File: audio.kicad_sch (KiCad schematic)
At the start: 14 parts

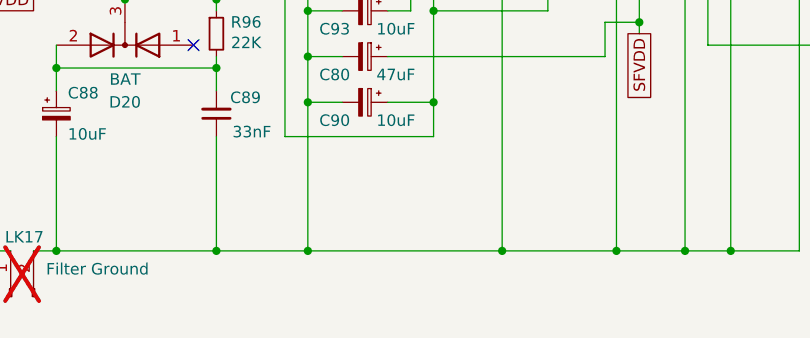
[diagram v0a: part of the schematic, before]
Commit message: add cheeky mean well power swap
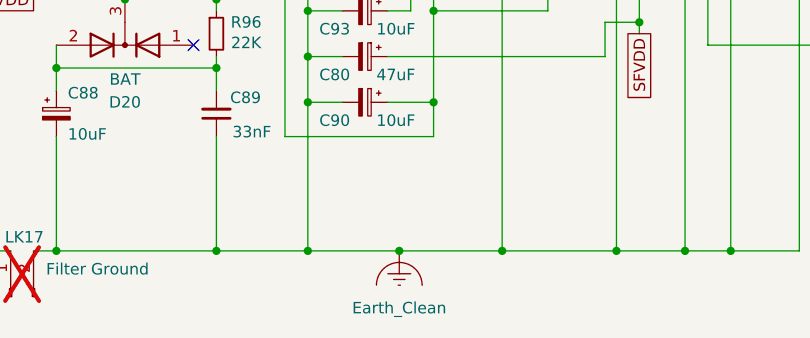
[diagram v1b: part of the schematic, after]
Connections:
- net Earth_Clean: now reaches C80.2, C88.2, C89.1, C90.2, C93.2, IM2.10 (Pin_10), IM2.13 (Pin_13), IM2.15 (Pin_15), IM2.18 (Pin_18), IM2.5 (Pin_5), LK17.2 (Pin_2), R212.2
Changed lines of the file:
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@@
+		(color 0 0 0 0)
+	)
+	(junction
+		(at 121.92 106.68)
+		(diameter 0)
 		(color 0 0 0 0)
 	)
@@
 	(wire
 		(pts
+			(xy 121.92 106.68) (xy 133.35 106.68)
+		)
+		(stroke
+			(width 0)
+			(type default)
+		)
+	)
+	(wire
+		(pts
 			(xy 166.37 66.04) (xy 166.37 106.68)
 		)
@@
 	(wire
 		(pts
-			(xy 111.76 106.68) (xy 133.35 106.68)
+			(xy 111.76 106.68) (xy 121.92 106.68)
 		)
 		(stroke
@@
 					(unit 1)
 				)
+			)
+		)
+	)
+	(symbol
+		(lib_id "power:Earth_Clean")
+		(at 121.92 106.68 0)
+		(unit 1)
+		(exclude_from_sim no)
+		(in_bom yes)
+		(on_board yes)
+		(dnp no)
+		(fields_autoplaced yes)
+		(property "Reference" "#PWR0199"
+			(at 121.92 114.3 0)
+			(effects
+				(font
+					(size 1.27 1.27)
+				)
+				(hide yes)
+			)
+		)
+		(property "Value" "Earth_Clean"
+			(at 121.92 113.03 0)
+			(effects
+				(font
+					(size 1.27 1.27)
+				)
+			)
+		)
+		(property "Footprint" ""
+			(at 121.92 107.95 0)
+			(effects
+				(font
+					(size 1.27 1.27)
+				)
+				(hide yes)
+			)
+		)
+		(property "Datasheet" "~"
+			(at 121.92 107.95 0)
+			(effects
+				(font
+					(size 1.27 1.27)
+				)
+				(hide yes)
+			)
+		)
+		(property "Description" "Power symbol creates a global label with name \"Earth_Clean\""
+			(at 121.92 106.68 0)
+			(effects
+				(font
+					(size 1.27 1.27)
+				)
+				(hide yes)
+			)
+		)
+		(pin "1"
+		)
+		(instances
+			(project "Acorn-A3010"
+				(path "/999882f3-94f8-4a89-9093-27a47d0cb289/0f9e4e4c-7eae-43dc-ad37-0c70003f4236"
+					(reference "#PWR0199")
+					(unit 1)
+				)

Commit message: fix port reference locations and lock components
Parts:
- C88, C90: footprint Capacitor_THT:CP_Radial_D4.0mm_P2.00mm -> Capacitor_THT:CP_Radial_D5.0mm_P2.50mm
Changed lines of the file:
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@@
 			)
 		)
-		(property "Footprint" "Capacitor_THT:CP_Radial_D4.0mm_P2.00mm"
+		(property "Footprint" "Capacitor_THT:CP_Radial_D5.0mm_P2.50mm"
 			(at 83.82 91.44 0)
 			(effects
@@
 			)
 		)
-		(property "Footprint" "Capacitor_THT:CP_Radial_D4.0mm_P2.00mm"
+		(property "Footprint" "Capacitor_THT:CP_Radial_D5.0mm_P2.50mm"
 			(at 118.11 90.17 0)
 			(effects

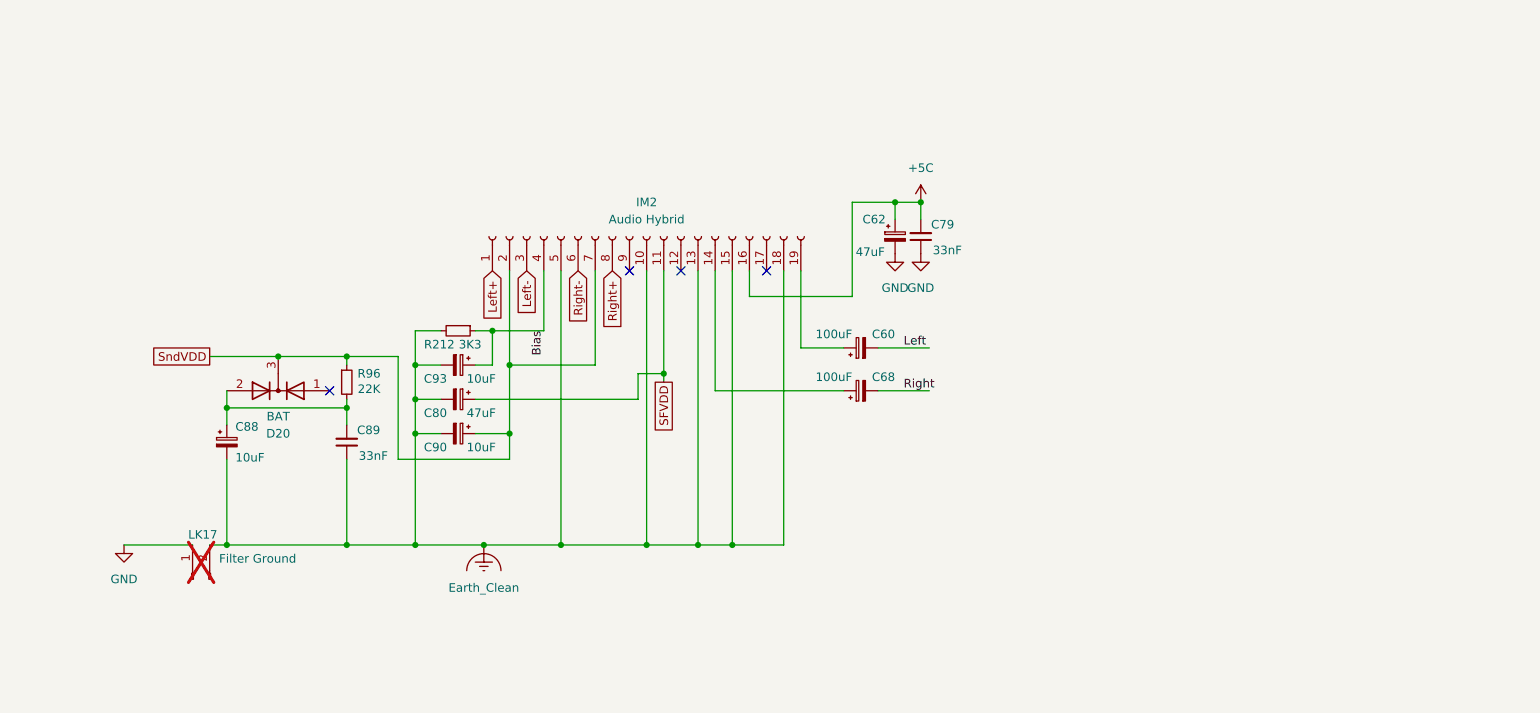
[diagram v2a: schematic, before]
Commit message: fix perimter port positions
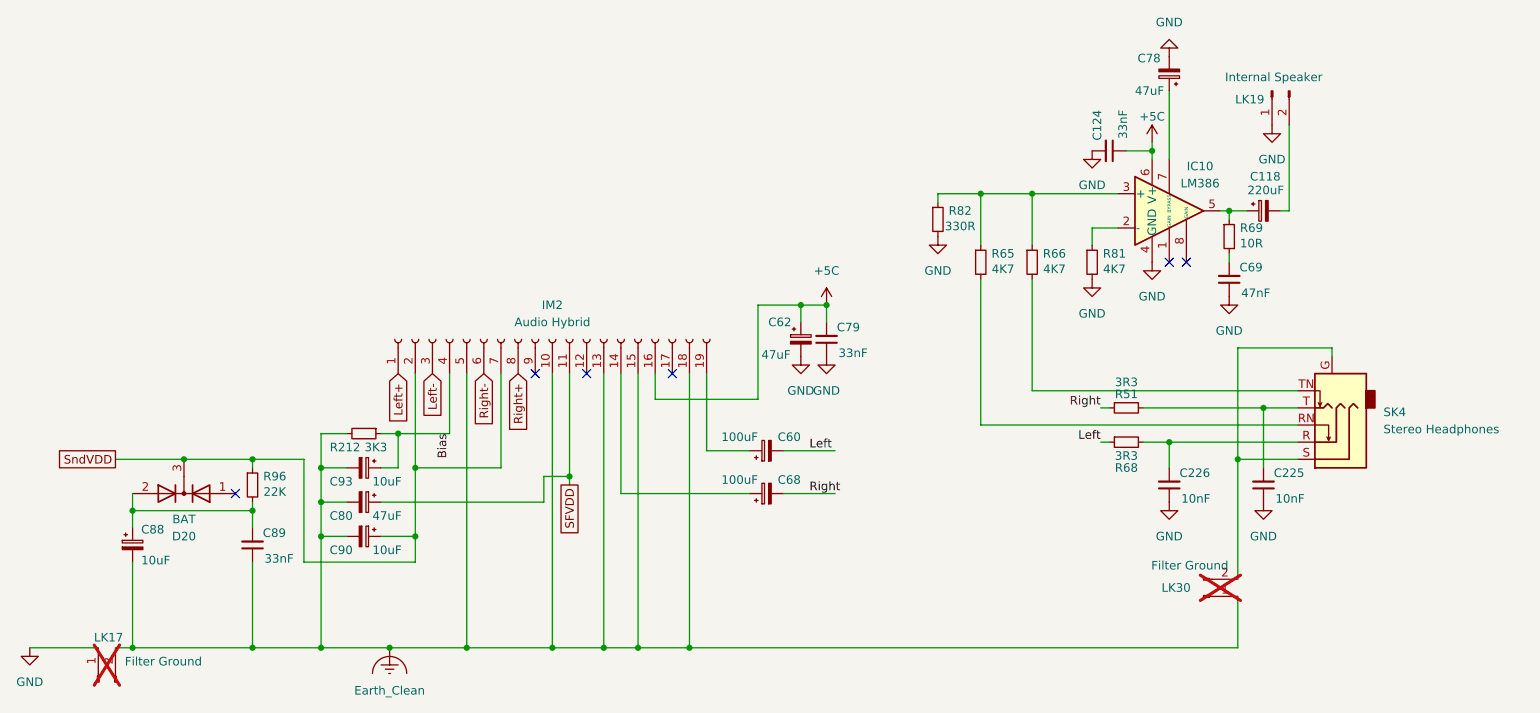
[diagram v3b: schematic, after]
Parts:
- added C118: 220uF, Capacitor_THT:CP_Radial_D8.0mm_P5.00mm, symbol Device:C_Polarized_Small
- added C124: 33nF, Capacitor_SMD:C_0805_2012Metric, symbol Device:C_Small
- added C225, C226: 10nF, Capacitor_SMD:C_0805_2012Metric, symbol Device:C_Small
- added C69: 47nF, Capacitor_SMD:C_0805_2012Metric, symbol Device:C_Small
- added C78: 47uF, Capacitor_THT:CP_Radial_D8.0mm_P5.00mm, symbol Device:C_Polarized_Small
- added IC10: LM386, Package_SO:SOIC-8_3.9x4.9mm_P1.27mm, symbol Amplifier_Audio:LM386
- added LK19: Internal Speaker, Connector_PinHeader_2.54mm:PinHeader_1x02_P2.54mm_Vertical, symbol Connector:Conn_01x02_Pin
- added LK30: Filter Ground, Connector_PinHeader_2.54mm:PinHeader_1x02_P2.54mm_Vertical, symbol Connector:Conn_01x02_Pin
- added R51, R68: 3R3, Resistor_SMD:R_0805_2012Metric, symbol Device:R_Small
- added R65, R66, R81: 4K7, Resistor_SMD:R_0805_2012Metric, symbol Device:R_Small
- added R69: 10R, Resistor_SMD:R_0805_2012Metric, symbol Device:R_Small
- added R82: 330R, Resistor_SMD:R_0805_2012Metric, symbol Device:R_Small
- added SK4: Stereo Headphones, Acorn:Jack_3.5mm_CUI_SJ1-3525N_Horizontal, symbol Connector_Audio:AudioJack3_Ground_SwitchTR
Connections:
- net +5C: now also C124.1, IC10.6 (V+)
- net Earth_Clean: now also LK30.1 (Pin_1)
- net GND: now also C124.2, C225.1, C226.1, C69.1, C78.2, IC10.4 (GND), LK19.1 (Pin_1), R81.2, R82.2
- net Left: now also R68.1
- net Right: now also R51.1
- new net: C225.2, R51.2, SK4.T
- new net: C69.2, R69.2
- new net: IC10.3 (+), R65.1, R66.1, R82.1
- new net: R65.2, SK4.RN
- new net: C118.1, IC10.5, R69.1
- new net: C118.2, LK19.2 (Pin_2)
- new net: R66.2, SK4.TN
- new net: IC10.2 (-), R81.1
- new net: C78.1, IC10.7 (BYPASS)
- new net: LK30.2 (Pin_2), SK4.G, SK4.S
- new net: C226.2, R68.2, SK4.R
- no-connect marks 4 -> 6
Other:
- moved on the sheet: C60, C62, C68, C79, C80, C88, C89, C90, C93, D20, IM2, LK17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

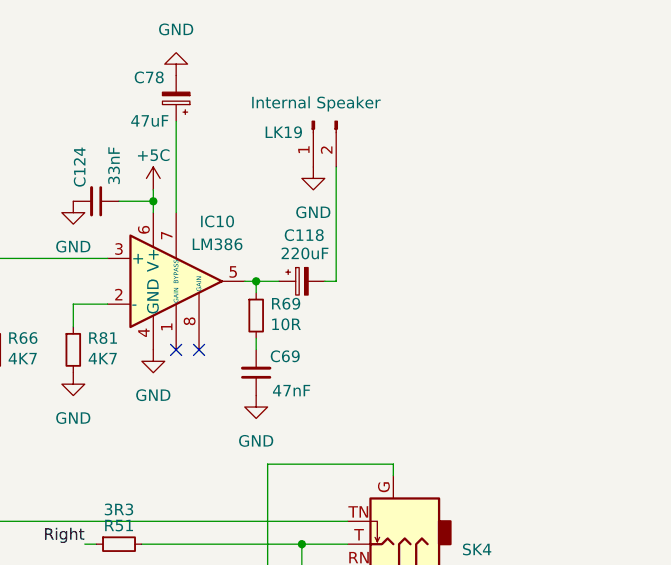
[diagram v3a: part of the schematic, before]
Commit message: add rf video output
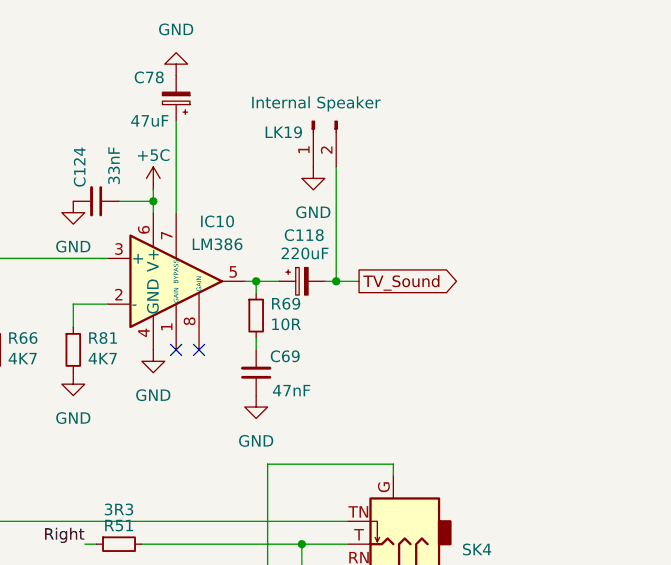
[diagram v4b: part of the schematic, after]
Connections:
- net TV_Sound: now reaches C118.2, LK19.2 (Pin_2)
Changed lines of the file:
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@@
+	)
+	(junction
+		(at 241.3 57.15)
+		(diameter 0)
+		(color 0 0 0 0)
 	)
 	(junction
@@
 		(pts
 			(xy 111.76 95.25) (xy 111.76 81.28)
+		)
+		(stroke
+			(width 0)
+			(type default)
+		)
+	)
+	(wire
+		(pts
+			(xy 241.3 57.15) (xy 243.84 57.15)
 		)
 		(stroke
@@
 				(hide yes)
 			)
+		)
+	)
+	(global_label "TV_Sound"
+		(shape output)
+		(at 243.84 57.15 0)
+		(fields_autoplaced yes)
+		(effects
+			(font
+				(size 1.27 1.27)
+			)
+			(justify left)
+		)
+		(property "Intersheetrefs" "${INTERSHEET_REFS}"
+			(at 255.6545 57.15 0)
+			(effects
+				(font
+					(size 1.27 1.27)
+				)
+				(justify left)
+				(hide yes)
+			)

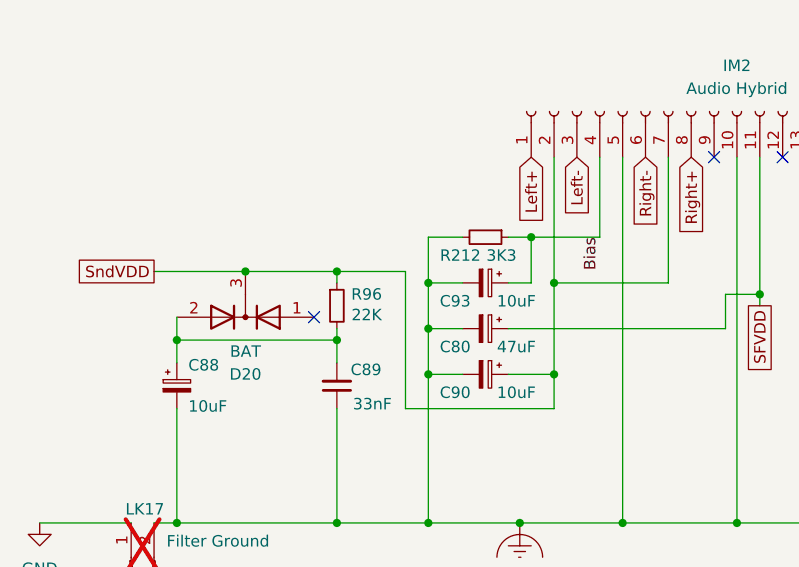
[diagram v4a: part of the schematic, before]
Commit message: video and keyboard routing
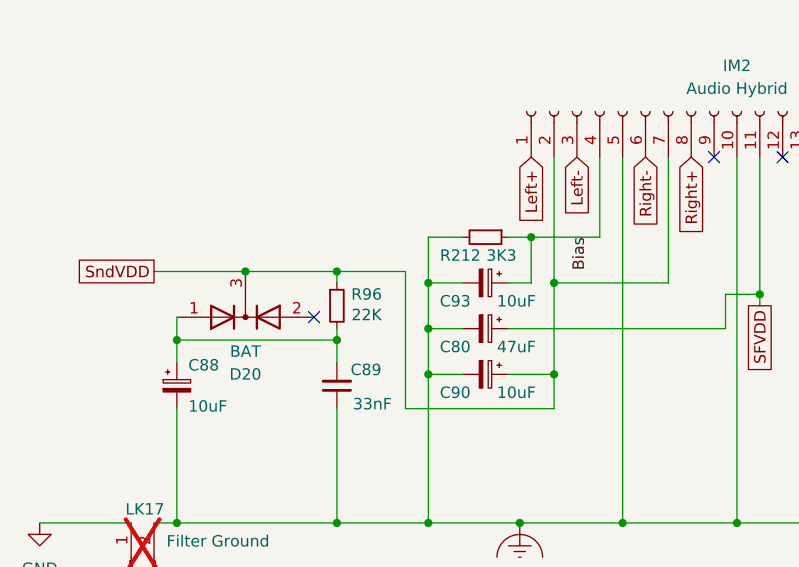
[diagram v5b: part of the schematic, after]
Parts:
- C88, C90: footprint Capacitor_THT:CP_Radial_D5.0mm_P2.50mm -> Capacitor_THT:CP_Radial_Tantal_D4.5mm_P5.00mm
- C93: footprint Capacitor_THT:CP_Radial_D4.0mm_P2.00mm -> Capacitor_THT:CP_Radial_Tantal_D4.5mm_P5.00mm
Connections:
- net at C88.1, C89.2, R96.2: now also D20.1 (A); no longer D20.2 (A)
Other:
- moved on the sheet: D20
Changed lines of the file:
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@@
 	)
 	(label "Bias"
-		(at 116.84 90.17 270)
+		(at 115.57 90.17 270)
 		(fields_autoplaced yes)
 		(effects
@@
 			)
 		)
-		(property "Footprint" "Capacitor_THT:CP_Radial_D5.0mm_P2.50mm"
+		(property "Footprint" "Capacitor_THT:CP_Radial_Tantal_D4.5mm_P5.00mm"
 			(at 69.85 106.68 0)
 			(effects
@@
 			)
 		)
-		(property "Footprint" "Capacitor_THT:CP_Radial_D4.0mm_P2.00mm"
+		(property "Footprint" "Capacitor_THT:CP_Radial_Tantal_D4.5mm_P5.00mm"
 			(at 104.14 95.25 0)
 			(effects
@@
 	(symbol
 		(lib_id "Device:D_Dual_CommonCathode_AAK")
-		(at 77.47 99.06 180)
+		(at 77.47 99.06 0)
+		(mirror x)
 		(unit 1)
 		(exclude_from_sim no)
@@
 			)
 		)
-		(property "Footprint" "Capacitor_THT:CP_Radial_D5.0mm_P2.50mm"
+		(property "Footprint" "Capacitor_THT:CP_Radial_Tantal_D4.5mm_P5.00mm"
 			(at 104.14 105.41 0)
 			(effects

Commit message: keyboard and joystick routing
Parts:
- C225, C226: now not fitted
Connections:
- net at R65.2: now also SK4.TN; no longer SK4.RN
- net at R66.2: now also SK4.RN; no longer SK4.TN
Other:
- moved on the sheet: R65, R66
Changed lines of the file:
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@@
 	)
 	(junction
-		(at 203.2 54.61)
-		(diameter 0)
-		(color 0 0 0 0)
-	)
-	(junction
 		(at 111.76 105.41)
 		(diameter 0)
@@
 	)
 	(junction
+		(at 195.58 54.61)
+		(diameter 0)
+		(color 0 0 0 0)
+	)
+	(junction
 		(at 144.78 121.92)
 		(diameter 0)
@@
 	)
 	(junction
-		(at 195.58 54.61)
+		(at 111.76 95.25)
 		(diameter 0)
 		(color 0 0 0 0)
 	)
 	(junction
-		(at 111.76 95.25)
+		(at 203.2 54.61)
 		(diameter 0)
 		(color 0 0 0 0)
@@
 	(wire
 		(pts
-			(xy 195.58 54.61) (xy 189.23 54.61)
+			(xy 189.23 54.61) (xy 195.58 54.61)
 		)
 		(stroke
@@
 	(wire
 		(pts
-			(xy 203.2 54.61) (xy 203.2 62.23)
+			(xy 220.98 46.99) (xy 220.98 48.26)
 		)
 		(stroke
@@
 	(wire
 		(pts
-			(xy 220.98 46.99) (xy 220.98 48.26)
+			(xy 195.58 67.31) (xy 195.58 88.9)
 		)
 		(stroke
@@
 	(wire
 		(pts
-			(xy 195.58 88.9) (xy 195.58 67.31)
-		)
-		(stroke
-			(width 0)
-			(type default)
-		)
-	)
-	(wire
-		(pts
 			(xy 132.08 81.28) (xy 132.08 121.92)
 		)
@@
 	(wire
 		(pts
-			(xy 203.2 67.31) (xy 203.2 83.82)
+			(xy 237.49 86.36) (xy 242.57 86.36)
 		)
 		(stroke
@@
 	(wire
 		(pts
-			(xy 237.49 86.36) (xy 242.57 86.36)
+			(xy 166.37 92.71) (xy 173.99 92.71)
 		)
 		(stroke
@@
 	(wire
 		(pts
-			(xy 166.37 92.71) (xy 173.99 92.71)
+			(xy 87.63 121.92) (xy 97.79 121.92)
 		)
 		(stroke
@@
 	(wire
 		(pts
-			(xy 87.63 121.92) (xy 97.79 121.92)
+			(xy 109.22 95.25) (xy 106.68 95.25)
 		)
 		(stroke
@@
 	(wire
 		(pts
-			(xy 109.22 95.25) (xy 106.68 95.25)
+			(xy 215.9 59.69) (xy 212.09 59.69)
 		)
 		(stroke
@@
 	(wire
 		(pts
-			(xy 215.9 59.69) (xy 212.09 59.69)
+			(xy 119.38 81.28) (xy 119.38 121.92)
 		)
 		(stroke
@@
 	(wire
 		(pts
-			(xy 119.38 81.28) (xy 119.38 121.92)
+			(xy 97.79 90.17) (xy 97.79 95.25)
 		)
 		(stroke
@@
 	(wire
 		(pts
-			(xy 97.79 90.17) (xy 97.79 95.25)
+			(xy 203.2 54.61) (xy 215.9 54.61)
 		)
 		(stroke
@@
 	(wire
 		(pts
-			(xy 215.9 54.61) (xy 203.2 54.61)
+			(xy 241.3 57.15) (xy 240.03 57.15)
 		)
 		(stroke
@@
 	(wire
 		(pts
-			(xy 241.3 57.15) (xy 240.03 57.15)
+			(xy 203.2 54.61) (xy 203.2 62.23)
 		)
 		(stroke
@@
 	(wire
 		(pts
-			(xy 144.78 121.92) (xy 139.7 121.92)
+			(xy 203.2 67.31) (xy 203.2 83.82)
 		)
 		(stroke
@@
 	(wire
 		(pts
-			(xy 69.85 101.6) (xy 87.63 101.6)
+			(xy 144.78 121.92) (xy 139.7 121.92)
 		)
 		(stroke
@@
 	(wire
 		(pts
-			(xy 168.91 71.12) (xy 172.72 71.12)
+			(xy 69.85 101.6) (xy 87.63 101.6)
 		)
 		(stroke
@@
 	(wire
 		(pts
-			(xy 189.23 54.61) (xy 189.23 55.88)
+			(xy 168.91 71.12) (xy 172.72 71.12)
 		)
 		(stroke
@@
 	(wire
 		(pts
-			(xy 233.68 121.92) (xy 233.68 114.3)
+			(xy 189.23 54.61) (xy 189.23 55.88)
 		)
 		(stroke
@@
 	(wire
 		(pts
-			(xy 69.85 99.06) (xy 69.85 101.6)
+			(xy 233.68 121.92) (xy 233.68 114.3)
 		)
 		(stroke
@@
 	(wire
 		(pts
-			(xy 223.52 91.44) (xy 242.57 91.44)
+			(xy 69.85 99.06) (xy 69.85 101.6)
 		)
 		(stroke
@@
 	(wire
 		(pts
-			(xy 203.2 54.61) (xy 195.58 54.61)
+			(xy 223.52 91.44) (xy 242.57 91.44)
 		)
 		(stroke
@@
 	(wire
 		(pts
+			(xy 195.58 54.61) (xy 195.58 62.23)
+		)
+		(stroke
+			(width 0)
+			(type default)
+		)
+	)
+	(wire
+		(pts
 			(xy 97.79 121.92) (xy 107.95 121.92)
 		)
@@
 	(wire
 		(pts
-			(xy 195.58 54.61) (xy 195.58 62.23)
-		)
-		(stroke
-			(width 0)
-			(type default)
-		)
-	)
-	(wire
-		(pts
 			(xy 111.76 95.25) (xy 124.46 95.25)
 		)
@@
 	(wire
 		(pts
+			(xy 195.58 54.61) (xy 203.2 54.61)
+		)
+		(stroke
+			(width 0)
+			(type default)
+		)
+	)
+	(wire
+		(pts
 			(xy 242.57 83.82) (xy 203.2 83.82)
 		)
@@
 		(in_bom yes)
 		(on_board yes)
-		(dnp no)
+		(dnp yes)
 		(property "Reference" "C225"
 			(at 239.014 96.012 0)
@@
 	(symbol
 		(lib_id "Device:R_Small")
-		(at 195.58 64.77 0)
+		(at 203.2 64.77 0)
 		(unit 1)
 		(exclude_from_sim no)
@@
 		(dnp no)
 		(property "Reference" "R65"
-			(at 198.882 63.5 0)
+			(at 206.502 63.5 0)
 			(effects
 				(font
@@
 		)
 		(property "Value" "4K7"
-			(at 198.882 65.786 0)
+			(at 206.502 65.786 0)
 			(effects
 				(font
@@
 		)
 		(property "Footprint" "Resistor_SMD:R_0805_2012Metric"
-			(at 195.58 64.77 0)
+			(at 203.2 64.77 0)
 			(effects
 				(font
@@
 		)
 		(property "Datasheet" "~"
-			(at 195.58 64.77 0)
+			(at 203.2 64.77 0)
 			(effects
 				(font
@@
 		)
 		(property "Description" "Resistor, small symbol"
-			(at 195.58 64.77 0)
+			(at 203.2 64.77 0)
 			(effects
 				(font
@@
 	(symbol
 		(lib_id "Device:R_Small")
-		(at 203.2 64.77 0)
+		(at 195.58 64.77 0)
 		(unit 1)
 		(exclude_from_sim no)
@@
 		(dnp no)
 		(property "Reference" "R66"
-			(at 206.502 63.5 0)
+			(at 198.882 63.5 0)
 			(effects
 				(font
@@
 		)
 		(property "Value" "4K7"
-			(at 206.502 65.786 0)
+			(at 198.882 65.786 0)
 			(effects
 				(font
@@
 		)
 		(property "Footprint" "Resistor_SMD:R_0805_2012Metric"
-			(at 203.2 64.77 0)
+			(at 195.58 64.77 0)
 			(effects
 				(font
@@
 		)
 		(property "Datasheet" "~"
-			(at 203.2 64.77 0)
+			(at 195.58 64.77 0)
 			(effects
 				(font
@@
 		)
 		(property "Description" "Resistor, small symbol"
-			(at 203.2 64.77 0)
+			(at 195.58 64.77 0)
 			(effects
 				(font
@@
 		(in_bom yes)
 		(on_board yes)
-		(dnp no)
+		(dnp yes)
 		(property "Reference" "C226"
 			(at 225.044 96.012 0)
